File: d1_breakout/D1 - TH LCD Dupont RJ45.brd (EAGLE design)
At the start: 43.5 x 43.8 mm, 17 parts, among them J1 RJ45-8X, Q1 2N7000, Q2 2N7000

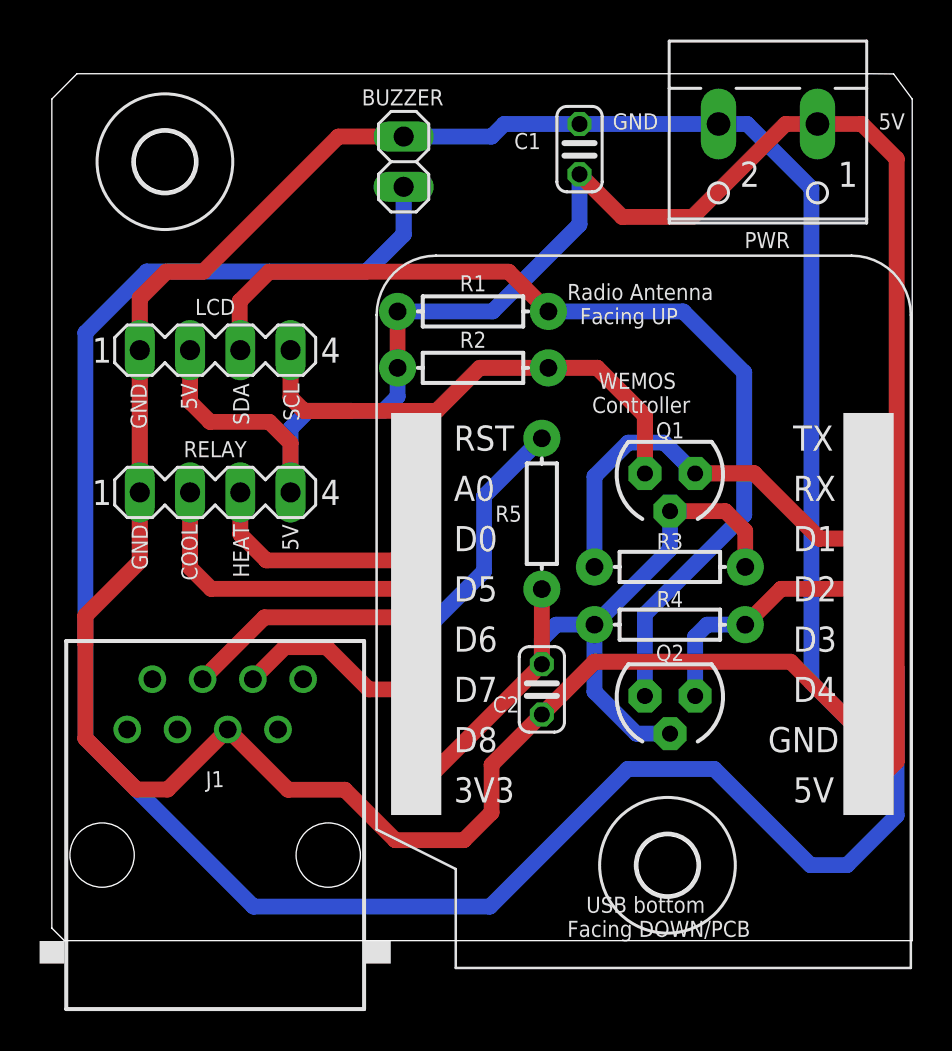
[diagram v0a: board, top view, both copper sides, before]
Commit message: Remove 90deg connection at power
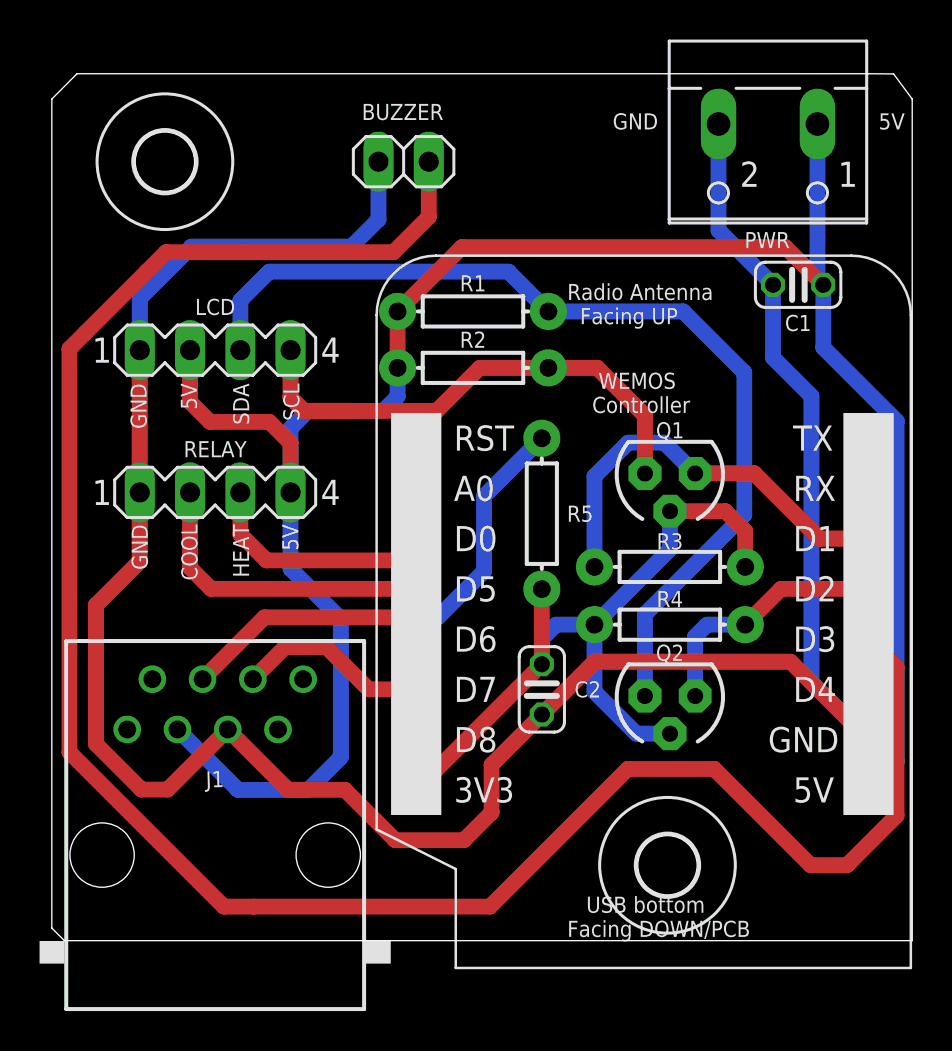
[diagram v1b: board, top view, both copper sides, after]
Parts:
- moved C1 13.0 mm to (77.7, 63.6), turned to 0 degrees
- turned BUZZER to 180 degrees
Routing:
- net 5V: track 90.3 -> 108.9 mm
- net GND: track 142.4 -> 124.7 mm
- net BZR: track 101.0 -> 104.6 mm
